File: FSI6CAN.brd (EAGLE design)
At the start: 35 x 49 mm, 32 parts, among them IC1 ATMEGA32M1, U1 MCP2551

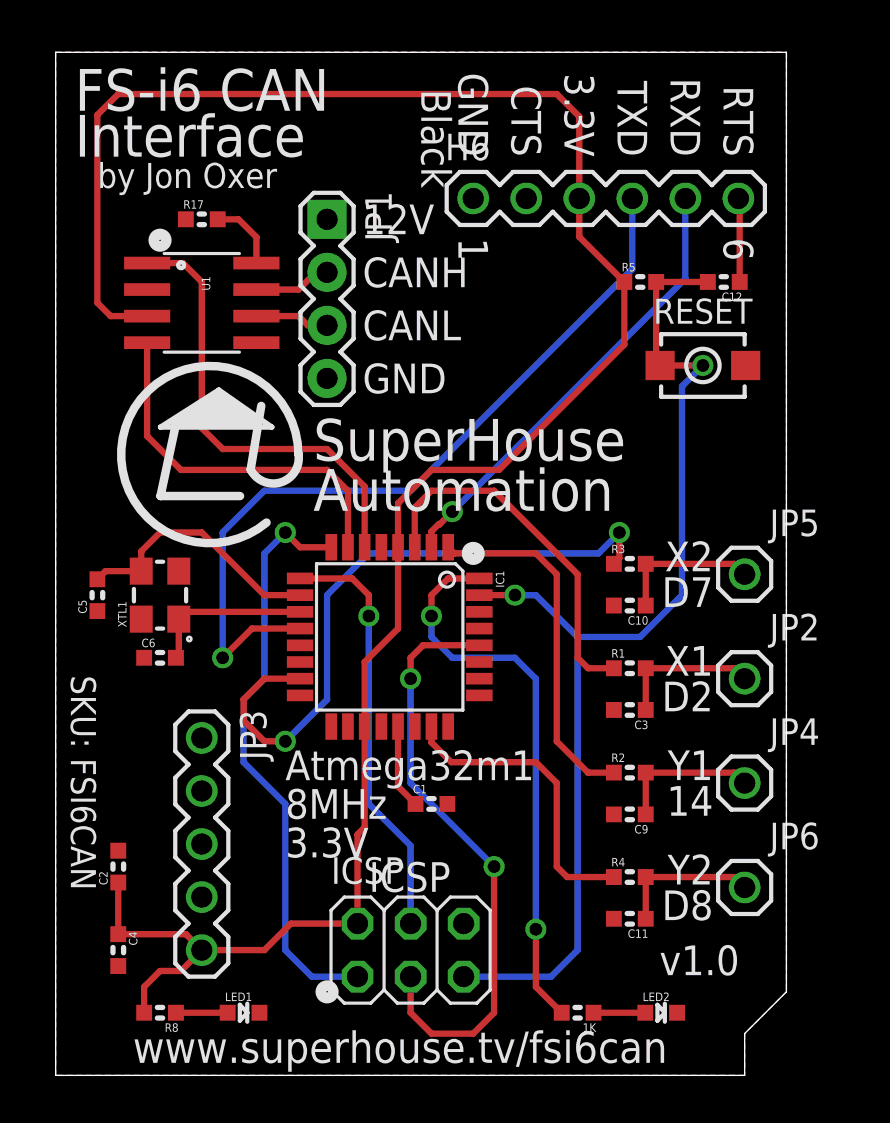
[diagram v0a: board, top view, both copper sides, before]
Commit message: Improved designators
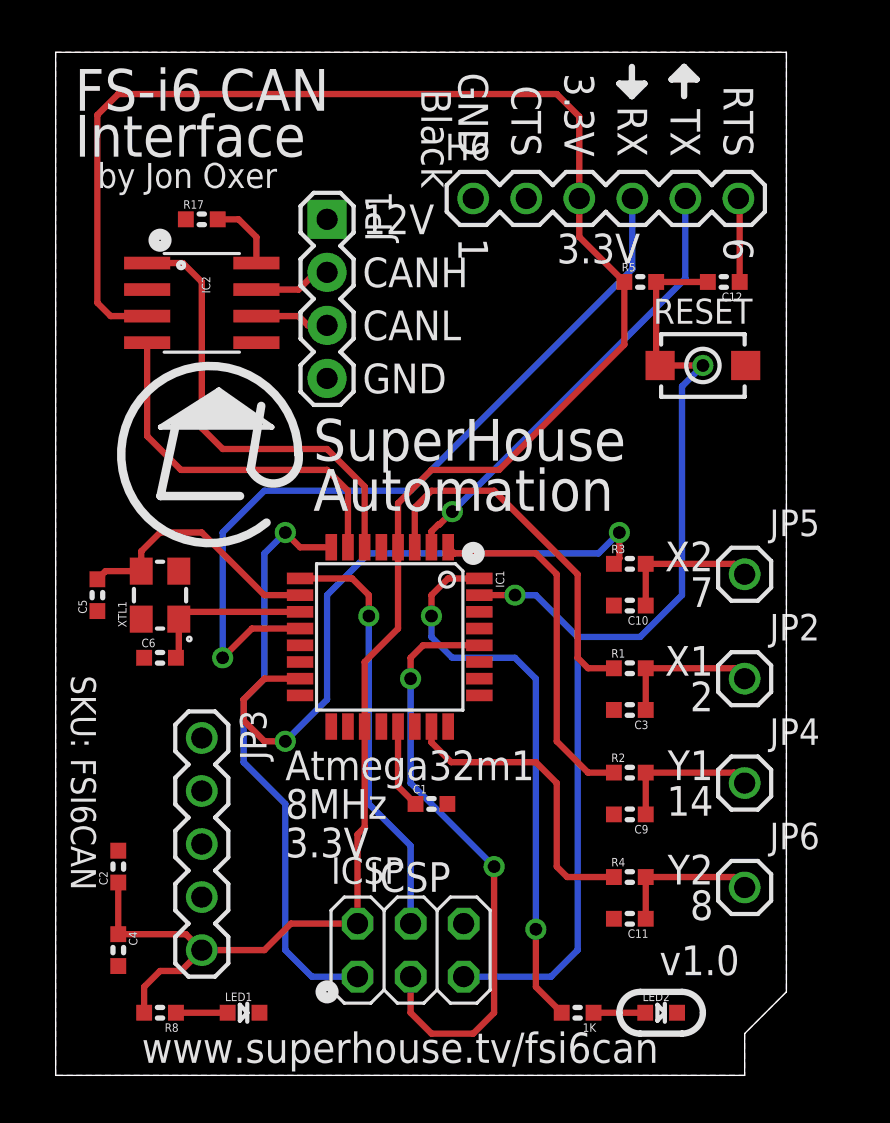
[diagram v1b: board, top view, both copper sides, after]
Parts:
- renumbered U1 to IC2
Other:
- board text added: "RX"
- board text added: "TX"
- board text added: "X1 2"
- board text added: "X2 7"
- board text added: "Y2 8"
- board text removed: "RXD"
- board text removed: "TXD"
- board text removed: "X1 D2"
- board text removed: "X2 D7"
- board text removed: "Y2 D8"

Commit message: Changed I/O pin for output Y2 and switch ICSP to other SPI port
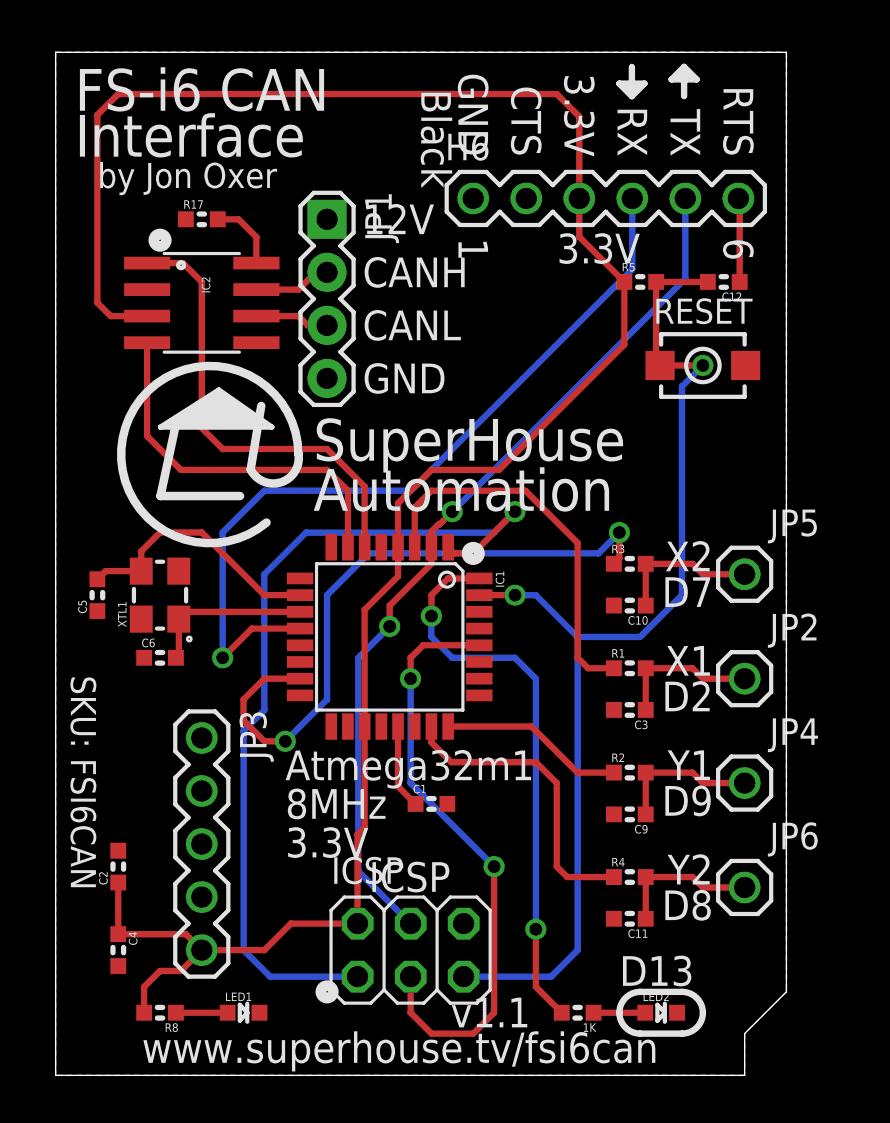
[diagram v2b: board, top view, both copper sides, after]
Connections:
- removed net D14: IC1.1, R2.1
- removed net D1_TX: H6.5, IC1.2
- new net D14_MISOA: IC1.1, ICSP.1
- new net D1_TX_MOSIA: H6.5, IC1.2, ICSP.4
- net D5_MISO: no longer ICSP.1
- net D6_MOSI: no longer ICSP.4
- net D9: now also R2.1
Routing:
- net D1_TX_MOSIA: track 0.00 -> 42.3 mm, vias 0 -> 2
- net D14_MISOA: track 0.00 -> 41.8 mm, vias 0 -> 1
- net D5_MISO: track 28.1 -> 0.00 mm, vias 1 -> 0
- net D1_TX: track 21.8 -> 0.00 mm, vias 1 -> 0
- net D6_MOSI: track 20.2 -> 0.00 mm, vias 1 -> 0
- net D14: track 17.1 -> 0.00 mm
- net D9: track 0.00 -> 8.85 mm
- net D2: track 17.6 -> 18.5 mm
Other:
- board text added: "D13"
- board text added: "X1 D2"
- board text added: "X2 D7"
- board text added: "Y1 D9"
- board text added: "Y2 D8"
- board text added: "v1.1"
- board text removed: "X1 2"
- board text removed: "X2 7"
- board text removed: "Y1 14"
- board text removed: "Y2 8"
- board text removed: "v1.0"

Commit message: Added CAN termination
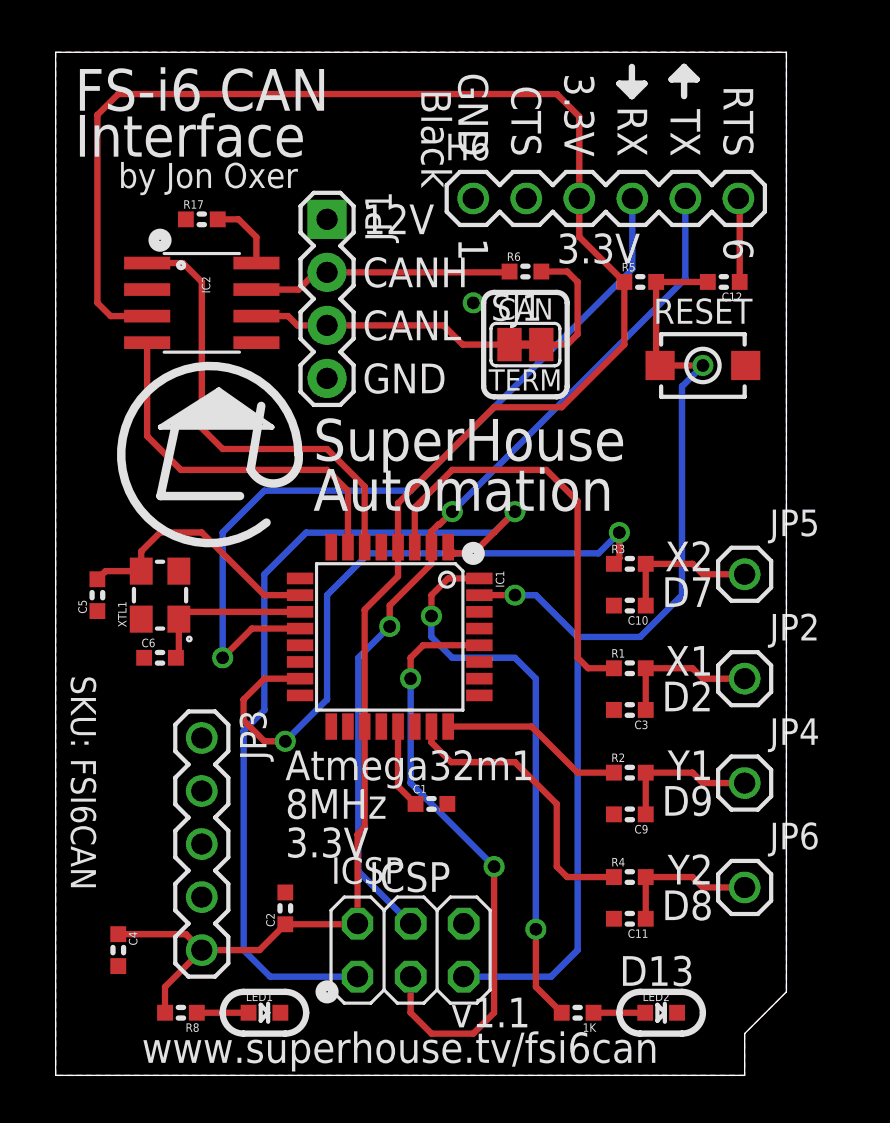
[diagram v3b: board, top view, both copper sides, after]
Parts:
- added R6: 120R, freetronics-master-v1.1:0603
- added SJ1: CAN Termination, freetronics-jon:SJC
- JP3: value (none) -> FS-i6
- moved C2 8.25 mm to (11.0, 8.00)
- moved LED1 1.00 mm to (10.0, 3.00)
- moved R8 1.00 mm to (6.00, 3.00)
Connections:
- new net N$2: R6.2, SJ1.2
- net CANH: now also R6.1
- net CANL: now also SJ1.1
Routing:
- net CANL: track 3.57 -> 12.7 mm
- net CANH: track 3.73 -> 12.5 mm
- net N$2: track 0.00 -> 6.39 mm
- net 3.3V: track 101.8 -> 98.4 mm
- net D2: track 18.5 -> 20.5 mm
- net D8: track 14.5 -> 13.9 mm
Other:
- board text added: "(C)2018-2019 SuperHouse Automation P/L"
- board text added: "CAN"
- board text added: "TERM"
- board text removed: "(C)2018 SuperHouse Automation P/L"

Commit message: Replaced MCP2551 with TCAN332DR
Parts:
- IC2: value MCP2551 -> TCAN332DR
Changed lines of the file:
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@@
 <attribute name="VALUE" x="8.984" y="3.5348" size="1.016" layer="27"/>
 </element>
-<element name="IC2" library="freetronics-original" package="SO08" value="MCP2551" x="7" y="37" smashed="yes" rot="R270">
+<element name="IC2" library="freetronics-original" package="SO08" value="TCAN332DR" x="7" y="37" smashed="yes" rot="R270">
 <attribute name="NAME" x="7" y="38.27" size="0.4064" layer="25" rot="R270"/>
 <attribute name="VALUE" x="4.23" y="32.865" size="1.016" layer="27"/>

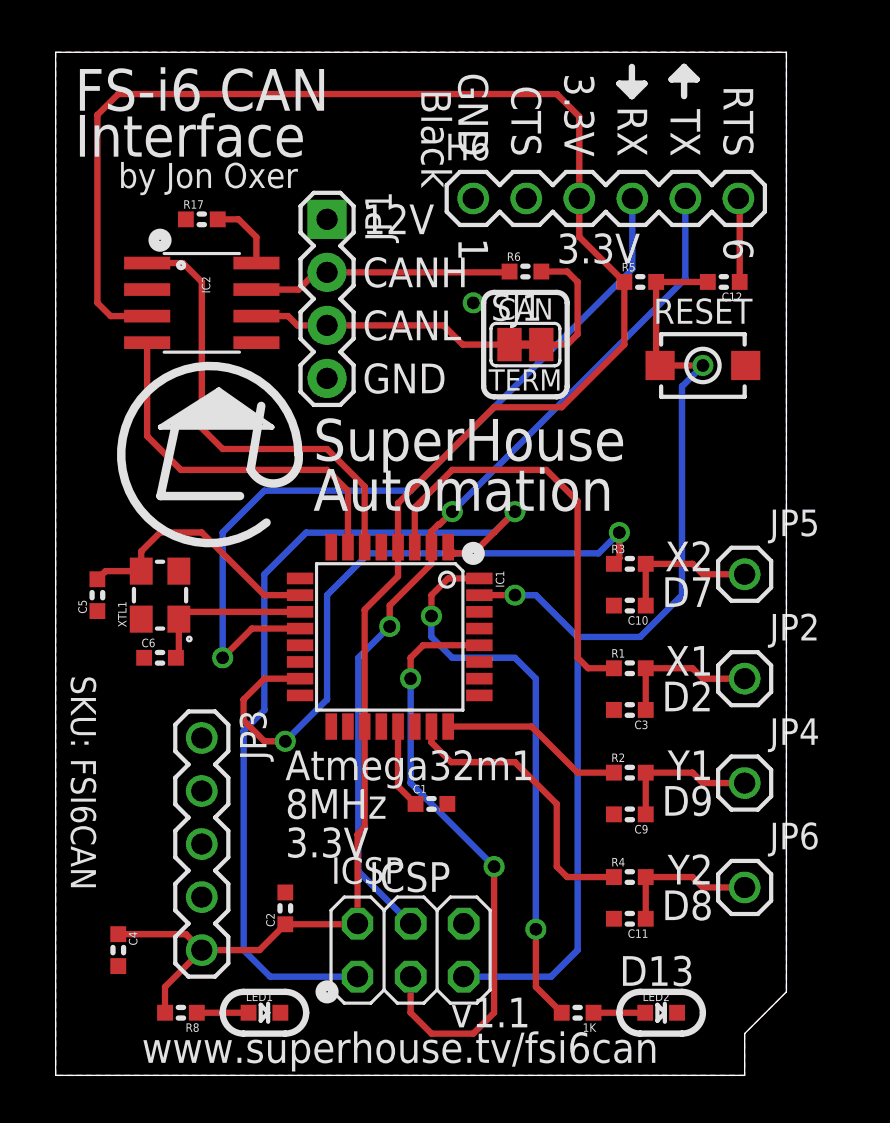
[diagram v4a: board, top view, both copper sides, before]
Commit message: Major rework using ATmega328p and MCP2515 for v2.0 release
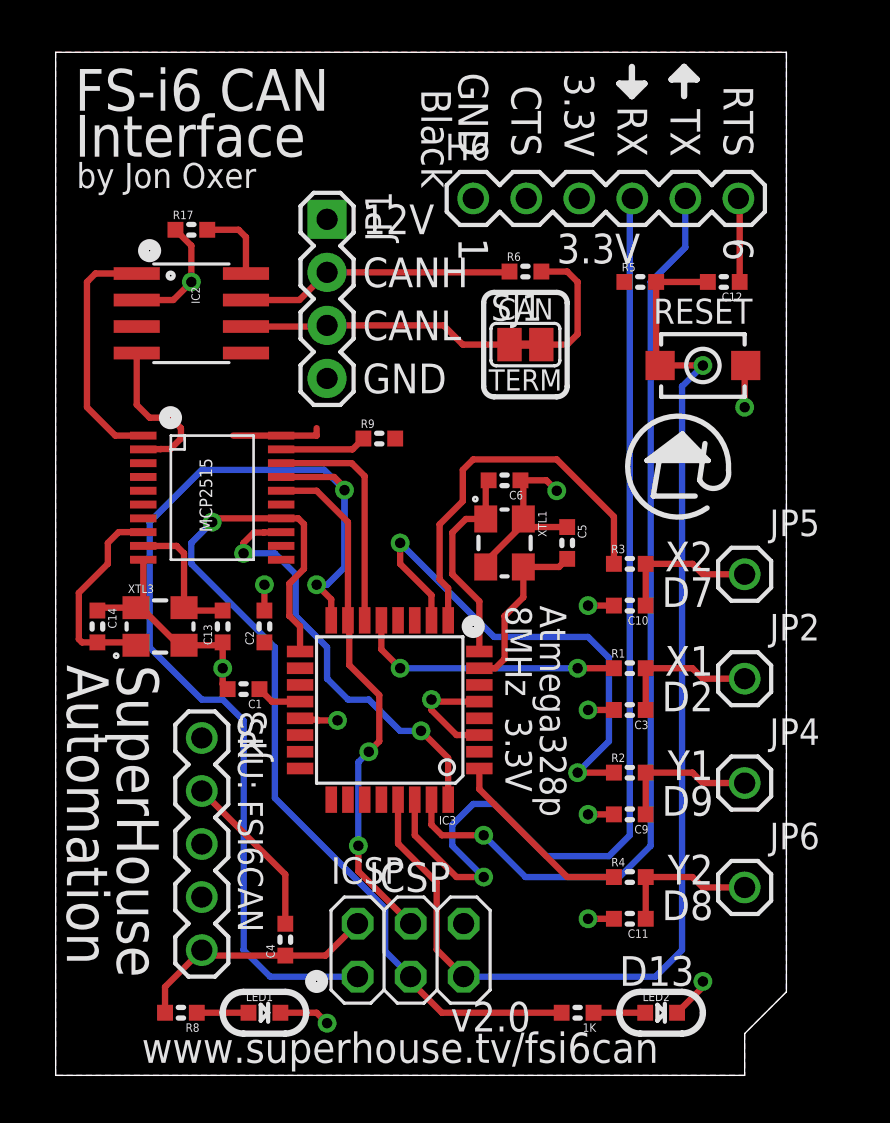
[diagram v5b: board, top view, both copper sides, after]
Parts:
- removed IC1: ATMEGA32M1, freetronics-jon:TQFP32-08
- added C13, C14: 15pF, freetronics-master-v1.1:0603
- added IC3: ATMEGA328P, freetronics-master-v1.1:TQFP32-08
- added IC4: MCP2515, MCP2515:TSSOP20
- added R9: 10K, freetronics-master-v1.1:0603
- added XTL3: 16MHz, freetronics-jon:CRYSTAL-SMD-3X2
- moved C5 22.6 mm to (24.5, 25.5), turned to 270 degrees
- moved C6 18.6 mm to (21.5, 28.5), turned to 180 degrees
- moved XTL1 16.7 mm to (21.5, 25.5), turned to 270 degrees
- moved C2 13.5 mm to (10.0, 21.5)
- moved C1 10.5 mm to (9.00, 18.5), turned to 180 degrees
- moved C4 8.02 mm to (11.0, 6.50), turned to 90 degrees
- moved IC2 0.71 mm to (6.50, 36.5)
- moved R17 0.71 mm to (6.50, 40.5)
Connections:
- removed net D10: IC1.25
- removed net D11: IC1.29
- removed net D12: IC1.30
- removed net D13: 1K.2, IC1.32
- removed net D14_MISOA: IC1.1, ICSP.1
- removed net D1_TX_MOSIA: H6.5, IC1.2, ICSP.4
- removed net D3_TXCAN: IC1.6, IC2.1
- removed net D4_RXCAN: IC1.7, IC2.4
- removed net D5_MISO: IC1.8
- removed net D6_MOSI: IC1.9
- removed net SCK: IC1.28, ICSP.3
- new net D10_SS: IC3.14, IC4.18
- new net D11_MOSI: IC3.15, IC4.16, ICSP.4
- new net D12_MISO: IC3.16, IC4.17, ICSP.1
- new net D13_SCK: 1K.2, IC3.17, IC4.14, ICSP.3
- new net D1_TX: H6.5, IC3.31
- new net D3: IC3.1, R4.1
- new net D4: IC3.2
- new net D5: IC3.9, R3.1
- new net D6: IC3.10, R2.1
- new net N$17: IC4.19, R9.1
- new net N$4: IC2.1, IC4.1
- new net N$6: IC2.4, IC4.2
- new net N$7: C13.2, IC4.9, XTL3.3
- new net N$8: C14.2, IC4.8, XTL3.1
- net 3.3V: now also IC3.18, IC3.4, IC3.6, IC4.20, R9.2; no longer IC1.19, IC1.4
- net A0: now also IC3.23; no longer IC1.13
- net A1: now also IC3.24; no longer IC1.14
- net A2: now also IC3.25; no longer IC1.16
- net A3: now also IC3.26; no longer IC1.17
- net A4: now also IC3.27; no longer IC1.18
- net A5: now also IC3.28; no longer IC1.22
- net A6: now also IC3.19; no longer IC1.26
- net A7: now also IC3.22; no longer IC1.27
- net AREF: now also IC3.20; no longer IC1.21
- net D0_RX: now also IC3.30; no longer IC1.12
- net D2: now also IC3.32, IC4.13; no longer IC1.3, R1.1
- net D7: now also IC3.11; no longer IC1.15, R3.1
- net D8: now also IC3.12; no longer IC1.23, R4.1
- net D9: now also IC3.13, R1.1; no longer IC1.24, R2.1
- net GND: now also C13.1, C14.1, IC3.21, IC3.3, IC3.5, IC4.10, XTL3.2, XTL3.4; no longer IC1.20, IC1.5
- net N$11: now also IC3.7; no longer IC1.10
- net N$12: now also IC3.8; no longer IC1.11
- net RESET: now also IC3.29; no longer IC1.31
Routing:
- net 3.3V: track 98.4 -> 16.3 mm
- net GND: track 0.00 -> 54.7 mm, vias 1 -> 13
- net D12_MISO: track 0.00 -> 50.7 mm, vias 0 -> 2
- net D13_SCK: track 0.00 -> 45.8 mm, vias 0 -> 1
- net D1_TX: track 0.00 -> 45.1 mm, vias 0 -> 1
- net D1_TX_MOSIA: track 42.3 -> 0.00 mm, vias 2 -> 0
- net D14_MISOA: track 41.8 -> 0.00 mm, vias 1 -> 0
- net D7: track 31.2 -> 0.00 mm, vias 2 -> 0
- net SCK: track 28.8 -> 0.00 mm, vias 2 -> 0
- net D13: track 27.0 -> 0.00 mm, vias 2 -> 0
- net D11_MOSI: track 0.00 -> 25.1 mm, vias 0 -> 2
- net D6: track 0.00 -> 24.5 mm, vias 0 -> 2
- net D3_TXCAN: track 21.9 -> 0.00 mm
- net D5: track 0.00 -> 18.7 mm
- net D4_RXCAN: track 17.9 -> 0.00 mm
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- added copper zone on layer 1, net 3.3V
- removed copper zone on layer 1, net GND
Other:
- board text added: "Atmega328p 8MHz 3.3V"
- board text added: "v2.0"
- board text removed: "Atmega32m1 8MHz 3.3V"
- board text removed: "v1.1"
